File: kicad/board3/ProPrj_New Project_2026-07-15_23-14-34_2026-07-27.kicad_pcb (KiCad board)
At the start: 4 copper layers, 250 x 50 mm, 143 parts, among them P1 WJ500V-5.08-2P, P2 WJ500V-5.08-2P, Q1 AO4406A, Q2 AO4406A, SW1 HX TS4538CJ 250gf 009, SW2 HX TS4538CJ 250gf 009, SW3 HX TS4538CJ 250gf 009, SW4 HX TS4538CJ 250gf 009, SW6 HX TS4538CJ 250gf 009, SW7 HX TS4538CJ 250gf 009, U1 STM32H755ZIT6, U11 AW9523BTQR, U12 AW9523BTQR, U2 W25Q512JVEIQ TR, U3 TPS563201DDCR, U4 CH224K, U5 LM74700QDBVRQ1, U6 LM74700QDBVRQ1, U7 FM24CL64B-GTR, U8 TJA1051T/3/1J, U9 TJA1051T/3/1J, X1 25MHz

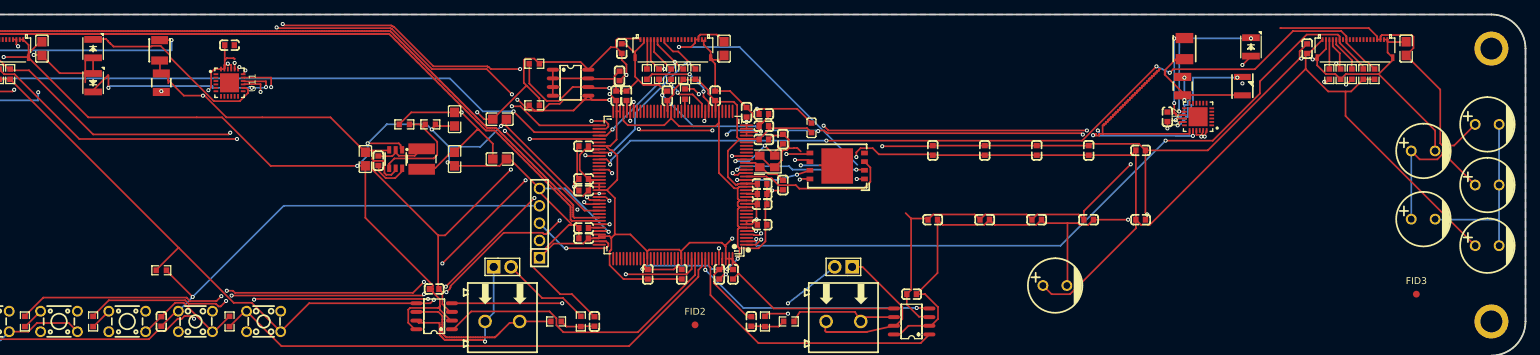
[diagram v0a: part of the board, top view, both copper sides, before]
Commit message: feat(kicad): U13 done + U14 partial -- SMD bulk conversion, 4/6 caps placed
U13 (schematic, netlist-verified): the six 220uF THT electrolytics are
deleted; the per-FPC 10uF becomes 22uF (C45783, JLC Basic, properties
swapped in place); six new caps added per the manufacturer's decoupling
spec -- 100nF at each FPC's BLVDD (C63-65) and 10uF at each FPC's 3V3
(C66-68). Each FPC already carried a 3V3 100nF (C17/18/19), so no
additions there. Total +5V bulk drops 880uF -> 66uF at the loads.

U14 (board, WIP): C63, C64, C65, C68 placed and stub-connected by a
collision-searching placer -- kicad_verify NEW=0, violations 35 < 36
baseline (one starved thermal resolved). Outstanding: C66 (FPC1) and
C67 (FPC2) have no legal pocket in the searched envelopes (south
fields are walled by VBUS_SENSE, the SCLK In2 river, and TT2's B-layer
run); 5 airwires pending until they are placed and connected. Fab
regen deferred until the board closes.

Co-Authored-By: Claude Fable 5 <noreply@anthropic.com>
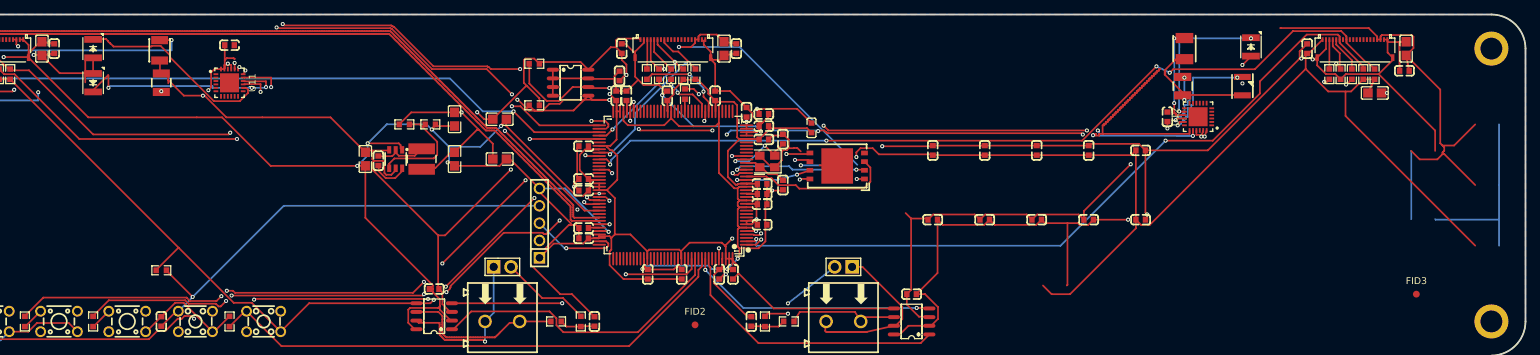
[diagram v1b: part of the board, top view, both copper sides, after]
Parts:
- removed C1, C12, C13, C14, C16, C2: ERS1EM221F12OT, ProPrj_New-easyedapro:CAP-TH_BD8.0-P3.50-D0.6-FD
- added C63: 100nF, C0603, F.Cu at (59.3, 90.0)
- added C64: 100nF, C0603, F.Cu at (159.3, 90.0)
- added C65: 100nF, C0603, F.Cu at (257.2, 93.2)
- added C68: 10uF, C0805, F.Cu at (252.9, 96.5)
- C29, C30, C31: value 10uF -> 22uF
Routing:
- net /GND: track 852.0 -> 861.7 mm, vias 25 -> 26
- net /+5V: track 415.4 -> 421.4 mm
- net /+3V3: track 570.1 -> 572.3 mm

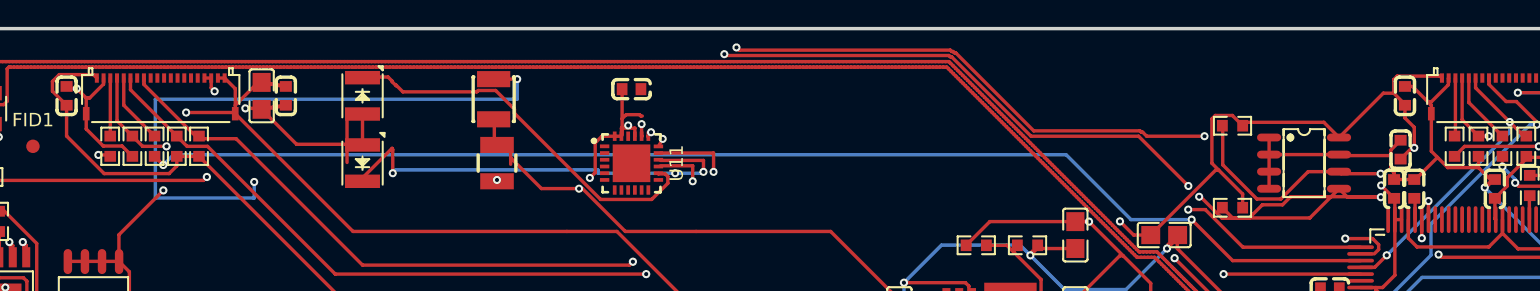
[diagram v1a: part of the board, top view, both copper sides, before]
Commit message: feat(kicad): U14 complete -- all six caps placed, fab regenerated
C66 lands at FPC1's south field (I1 hop over the VBUS_SENSE top-layer
run, GND via clear of TT2's B route); C67 lands in FPC2's north band
(no USB serpentines there), rail stub straight into FPC2 pin 1. Both
validated element-by-element with exact clearance math before placement.
kicad_verify: NEW=0, 35 violations (one under the pre-U13 baseline).

The 5 remaining unconnected items are legacy, now fully diagnosed for
the finisher: 2x /+5V chains lost their layer junctions when the THT
cans' through-hole pads were deleted (fix: junction vias at
(258.25,105) and on the y86.99 horizontal -- both spots verified
covered by the In2 +5V fill); 3x F-zone GND fragment pairs, including
U11's EP fragment whose every via-legal latitude is blocked by the
VBUS_SENSE/MISO/MOSI/TT5 river stack (needs a fill-bridge or micro-via
decision, not a standard stitch).

Co-Authored-By: Claude Fable 5 <noreply@anthropic.com>
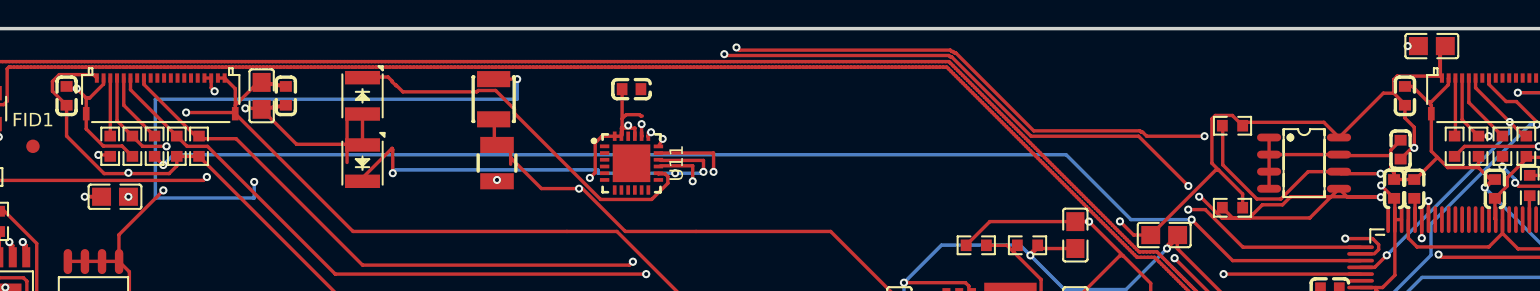
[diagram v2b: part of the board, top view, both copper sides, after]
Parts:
- added C66: 10uF, C0805, F.Cu at (46.6, 97.5)
- added C67: 10uF, C0805, F.Cu at (144.5, 86.3)
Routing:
- net /+3V3: track 572.3 -> 576.8 mm, vias 10 -> 12
- net /GND: track 861.7 -> 863.9 mm, vias 26 -> 28

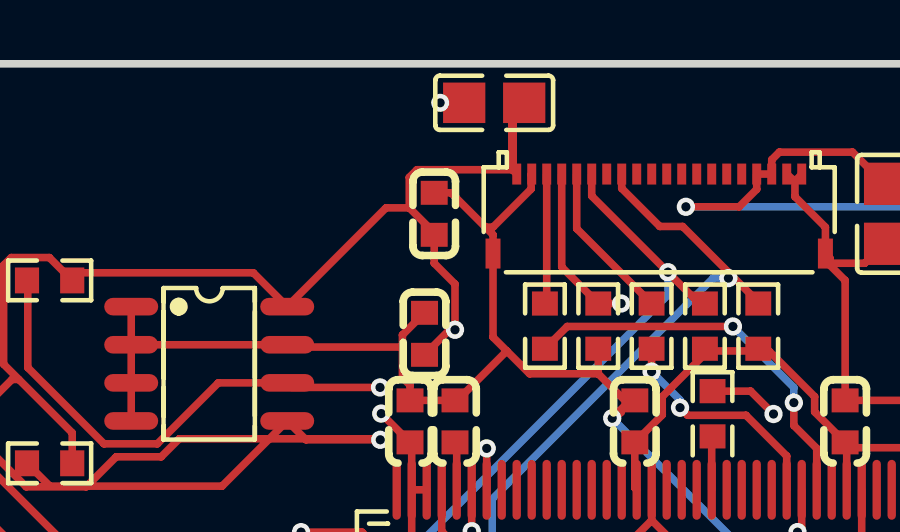
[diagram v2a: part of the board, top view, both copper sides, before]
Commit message: fix(kicad): C67 out of FPC2's FFC insertion path
Kevin caught it on review: C67 sat 0.32 mm from FPC2's north face --
directly in the flat-flex ribbon's approach, which DRC cannot see.
Relocated to the west pocket at (140.35, 92.70) as a 0603 10uF
(C19702, JLC Basic; ~8uF effective at 3.3V, inside the 4.7-10uF spec)
since the 0805 fits no south pocket. Standing rule for this board: the
strip between each FPC's north face and the board edge is cable
territory -- no components. Gates unchanged: NEW=0, 35 violations,
airwires the 5 diagnosed legacy items.

Co-Authored-By: Claude Fable 5 <noreply@anthropic.com>
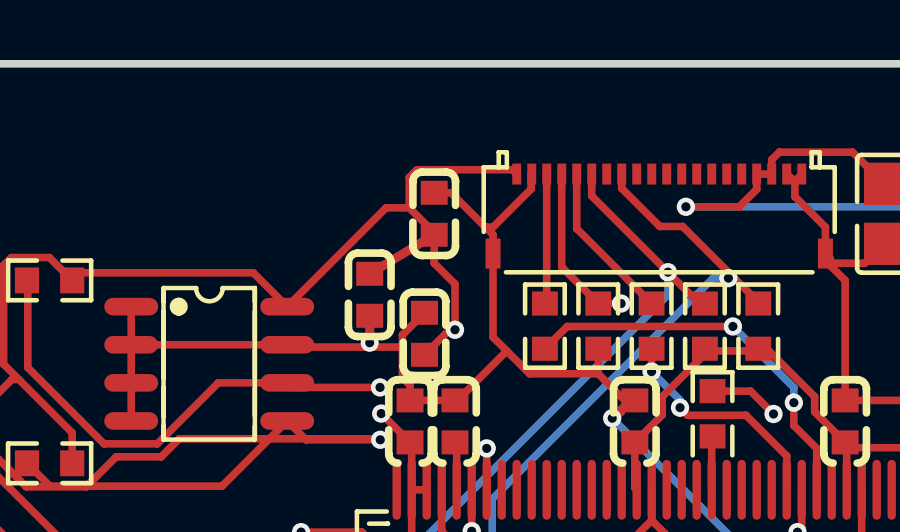
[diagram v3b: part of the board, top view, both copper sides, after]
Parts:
- C67: footprint C0805 -> C0603
- moved C67 7.63 mm to (140.3, 92.7), turned to -90 degrees

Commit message: fix(kicad): close all five airwires -- board fully connected, 0 unconnected
All five were THT-deletion artifacts or long-standing under-stitching:
- 2x /+5V: the deleted cans' through-hole pads were the layer junctions;
  junction vias restored at (258.25,105) and (239.5,86.99), both spots
  verified covered by the In2 +5V plane.
- 12 GND stitching vias bond every top-layer fill fragment that had no
  via of its own (each spot grid-searched, clearance-checked, and
  required to land on In1 fill).
- U11's ground cluster (EP + pad 9) sat sealed under five signal rivers
  with no legal via latitude. Freed by rerouting TT1's east web south
  (y97.7 -> y99.6 -- the west join is colinear with its existing 45-deg
  diagonal, so the reroute is a pure extension), opening a south exit
  from pad 9 between the row pads to a via at (84.95,99.05).

kicad_verify: 0 unconnected (was 5), NEW=0, 35 violations = the
running baseline. Fab package regenerated.

Co-Authored-By: Claude Fable 5 <noreply@anthropic.com>
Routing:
- net /TT1_LED_K: track 28.7 -> 31.4 mm
- net /GND: track 863.9 -> 865.8 mm, vias 28 -> 41
- net /+5V: vias 16 -> 18
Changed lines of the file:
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@@
 				(font
 					(size 1.27 1.27)
+					(thickness 0.15)
 				)
 			)
@@
 				(font
 					(size 1.27 1.27)
+					(thickness 0.15)
 				)
 			)
@@
 	)
 	(segment
+		(start 84.75 98.85)
+		(end 84.95 99.05)
+		(width 0.254)
+		(layer "F.Cu")
+		(net "/GND")
+	)
+	(segment
 		(start 31.712 103.708)
 		(end 31.712 104.3185)
@@
 	)
 	(segment
+		(start 84.75 97.32)
+		(end 84.75 98.85)
+		(width 0.254)
+		(layer "F.Cu")
+		(net "/GND")
+	)
+	(segment
 		(start 141.44 94.441)
 		(end 137.676 94.441)
@@
 	)
 	(via
+		(at 108.7 109.6)
+		(size 0.6)
+		(drill 0.3)
+		(layers "F.Cu" "B.Cu")
+		(net "/GND")
+	)
+	(via
+		(at 92.8 132.9)
+		(size 0.6)
+		(drill 0.3)
+		(layers "F.Cu" "B.Cu")
+		(net "/GND")
+	)
+	(via
+		(at 243.8 89.1)
+		(size 0.6)
+		(drill 0.3)
+		(layers "F.Cu" "B.Cu")
+		(net "/GND")
+	)
+	(via
+		(at 223.3 101.5)
+		(size 0.6)
+		(drill 0.3)
+		(layers "F.Cu" "B.Cu")
+		(net "/GND")
+	)
+	(via
 		(at 180.691 104.3165)
 		(size 0.61)
@@
 	)
 	(via
+		(at 32.799999 106.1)
+		(size 0.6)
+		(drill 0.3)
+		(layers "F.Cu" "B.Cu")
+		(net "/GND")
+	)
+	(via
+		(at 28.7 108)
+		(size 0.6)
+		(drill 0.3)
+		(layers "F.Cu" "B.Cu")
+		(net "/GND")
+	)
+	(via
 		(at 164.543 110.813)
 		(size 0.61)
@@
 	)
 	(via
+		(at 84.95 99.05)
+		(size 0.6)
+		(drill 0.3)
+		(layers "F.Cu" "B.Cu")
+		(net "/GND")
+	)
+	(via
+		(at 136.6 106.1)
+		(size 0.6)
+		(drill 0.3)
+		(layers "F.Cu" "B.Cu")
+		(net "/GND")
+	)
+	(via
 		(at 44.35 97.5)
 		(size 0.6)
@@
 	)
 	(via
+		(at 117.6 125.8)
+		(size 0.6)
+		(drill 0.3)
+		(layers "F.Cu" "B.Cu")
+		(net "/GND")
+	)
+	(via
 		(at 116.982 106.684)
 		(size 0.61)
@@
 	)
 	(via
+		(at 213.6 101.7)
+		(size 0.6)
+		(drill 0.3)
+		(layers "F.Cu" "B.Cu")
+		(net "/GND")
+	)
+	(via
 		(at 159.506 120.8)
 		(size 0.61)
@@
 	)
 	(via
+		(at 156.1 124.6)
+		(size 0.6)
+		(drill 0.3)
+		(layers "F.Cu" "B.Cu")
+		(net "/GND")
+	)
+	(via
+		(at 164.7 100.5)
+		(size 0.6)
+		(drill 0.3)
+		(layers "F.Cu" "B.Cu")
+		(net "/GND")
+	)
+	(via
 		(at 242.14 91.458)
 		(size 0.61)
@@
 	)
 	(via
+		(at 125.7 101.4)
+		(size 0.6)
+		(drill 0.3)
+		(layers "F.Cu" "B.Cu")
+		(net "/GND")
+	)
+	(via
 		(at 105.253 103.89)
 		(size 0.61)
@@
 	)
 	(via
+		(at 258.25 105)
+		(size 0.6)
+		(drill 0.3)
+		(layers "F.Cu" "B.Cu")
+		(net "/+5V")
+	)
+	(via
 		(at 81.1 96.9)
 		(size 0.6)
@@
 	)
 	(via
+		(at 239.5 86.99)
+		(size 0.6)
+		(drill 0.3)
+		(layers "F.Cu" "B.Cu")
+		(net "/+5V")
+	)
+	(via
 		(at 233.5 95.1)
 		(size 0.6)
@@
 	)
 	(segment
+		(start 84.6 99.6)
+		(end 86.85 99.6)
+		(width 0.254)
+		(layer "F.Cu")
+		(net "/TT1_LED_K")
+	)
+	(segment
 		(start 73.5 89.7)
 		(end 68 89.7)
@@
 	)
 	(segment
-		(start 82.7 97.7)
-		(end 76.3 91.3)
+		(start 76.3 91.3)
+		(end 76.3 91)
 		(width 0.254)
 		(layer "F.Cu")
@@
 	)
 	(segment
-		(start 76.3 91.3)
-		(end 76.3 91)
+		(start 86.85 99.6)
+		(end 87.7 96.5)
 		(width 0.254)
 		(layer "F.Cu")
@@
 	)
 	(segment
-		(start 67.5 89.2)
-		(end 67.5 89.2465)
+		(start 76.3 91.3)
+		(end 84.6 99.6)
 		(width 0.254)
 		(layer "F.Cu")
@@
 	)
 	(segment
-		(start 87.5 95.8)
-		(end 87 95.8)
+		(start 67.5 89.2)
+		(end 67.5 89.2465)
 		(width 0.254)
 		(layer "F.Cu")
@@
 	)
 	(segment
-		(start 87.7 96.5)
-		(end 86.5 97.7)
+		(start 87.5 95.8)
+		(end 87 95.8)
 		(width 0.254)
 		(layer "F.Cu")
@@
 		(width 0.254)
 		(layer "F.Cu")
-		(net "/TT1_LED_K")
-	)
-	(segment
-		(start 86.5 97.7)
-		(end 82.7 97.7)
-		(width 0.254)
-		(layer "F.Cu")
